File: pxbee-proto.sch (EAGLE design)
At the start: 2 parts

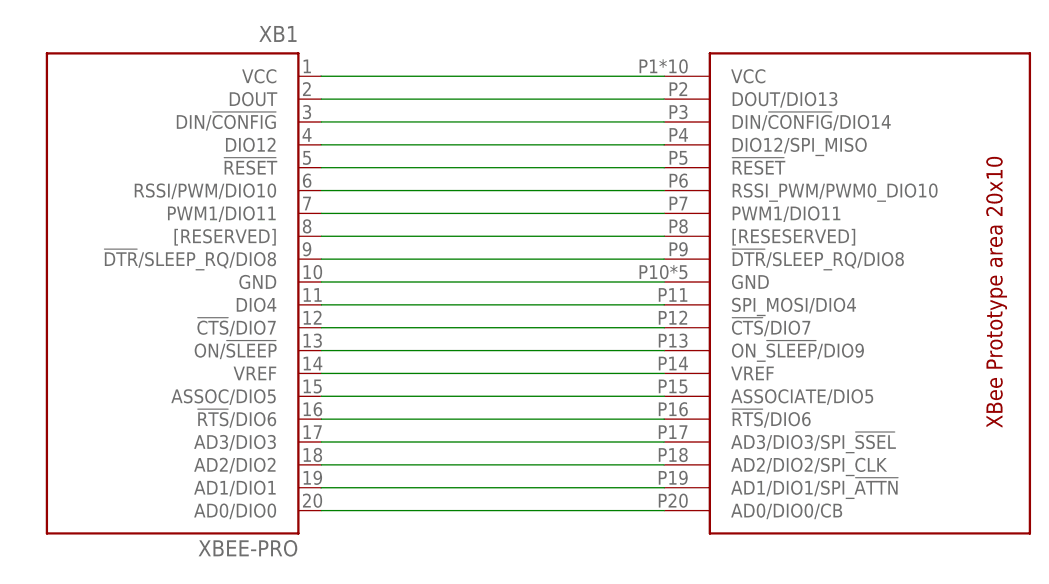
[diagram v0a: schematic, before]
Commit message: Update prototype component; Mark VCC and GND area
- VCC and GND area are now marked in silkscreen layer
- Addresses findings in #1
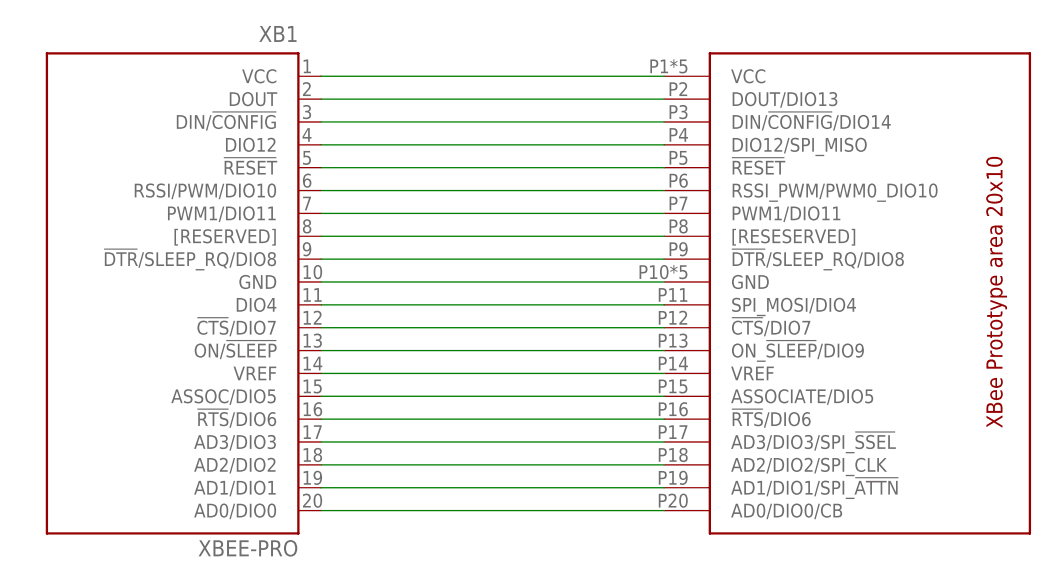
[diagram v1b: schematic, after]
